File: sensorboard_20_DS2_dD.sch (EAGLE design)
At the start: 107 parts, among them IC1 ECMF02-2AMX6, IC2_ESP32S2WROOMM22S2 ESP32-S2-WROOM_M22S2H3200PH3Q0, IC4 TPA6211A1DRBR, J4_USB USB_CONN, J5_AUDIO SJ-3523-SMT-TR, J6_OAT 2.5mm JACK, J7 30310-6002HB, U1 LPS22HB, U10-MAG_SENSOR MMC5983MA, U11 LDL212PV33R, U12 NCV8163ASN330T1G, U13-I2C DS2482S-100+, U2 LPS22HB, U3-IMU LSM6DSMTR, U4 NCV8163ASN330T1G, U5 NCV8163ASN330T1G, U6 NCV8163ASN330T1G, U7 NCV8163ASN330T1G

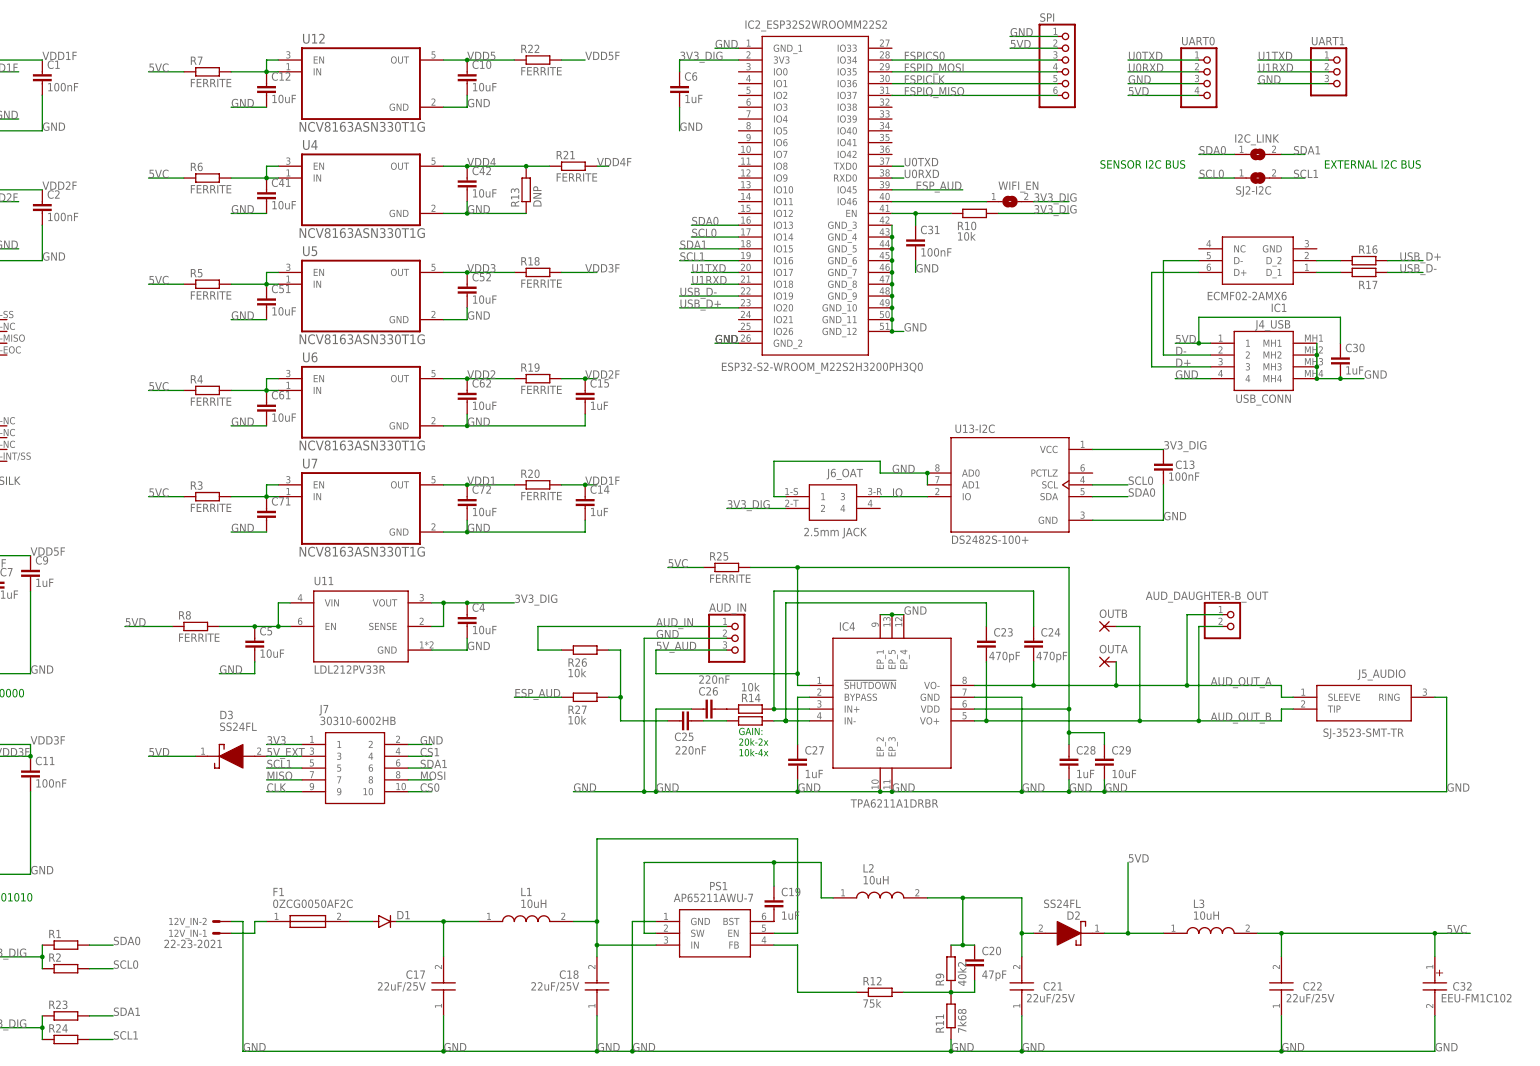
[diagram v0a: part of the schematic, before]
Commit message: Upload v20 files
Extend UART0 connector with EN, GPIO0 pins (Fixes #2)
Move ESP_AUD, WIFI_EN to different ESP32 pins (Fixes #3)
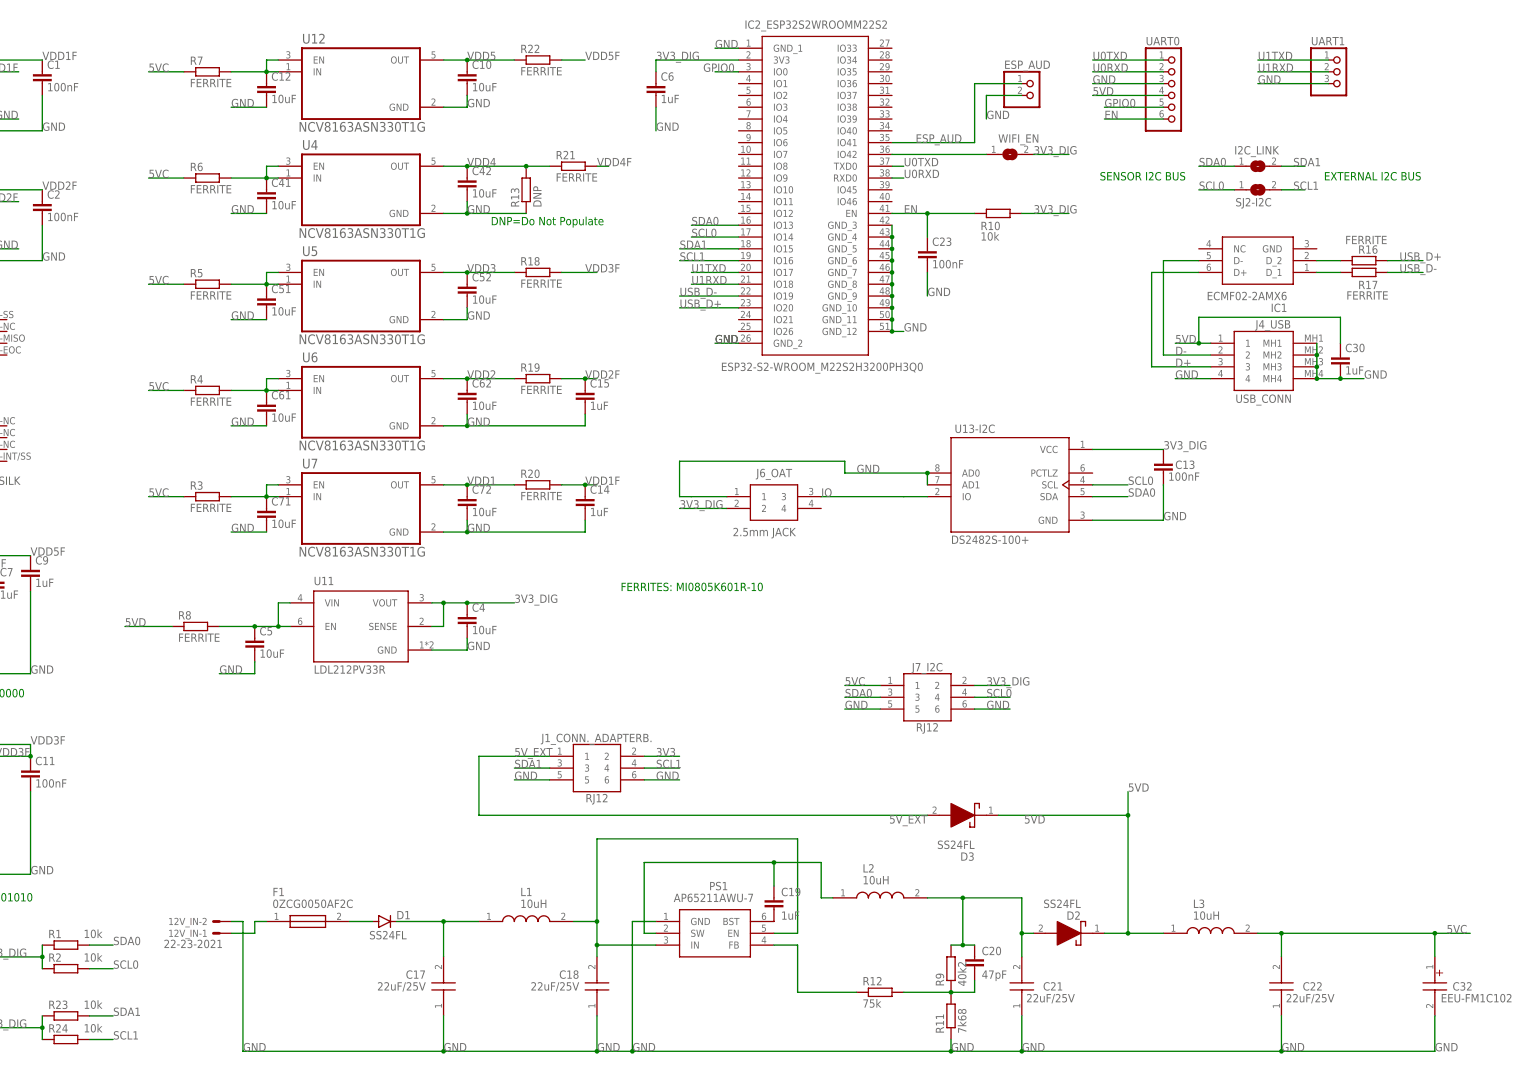
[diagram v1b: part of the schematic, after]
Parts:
- removed AUD_DAUGHTER-B_OUT: (no value), pinhead:PINHD-1X2
- removed AUD_IN: (no value), pinhead:PINHD-1X3
- removed C24: 470pF, rcl:C-EUC0805
- removed C25, C26: 220nF, rcl:C-EUC1206
- removed C27, C28: 1uF, rcl:C-EUC1206
- removed C29: 10uF, rcl:C-EUC1206
- removed C31: 100nF, rcl:C-EUC0603
- removed IC4: TPA6211A1DRBR, SamacSys_Parts:TPA6211A1DRBR
- removed J5_AUDIO: SJ-3523-SMT-TR, SamacSys_Parts:SJ-3523-SMT-TR
- removed J7: 30310-6002HB, SamacSys_Parts:30310-6002HB
- removed OUTA, OUTB: (no value), wirepad_SMALL:SMD2_SMALLSMALL
- removed R14, R26, R27: 10k, rcl:R-EU_R0805
- removed R15: (no value), rcl:R-EU_R0805
- removed R25: FERRITE, rcl:R-EU_R0805
- removed SPI: (no value), pinhead_dD:PINHD-1X6
- added ESP_AUD: (no value), pinhead:PINHD-1X2
- added J1_CONN._ADAPTERB., J7_I2C: RJ12, Sensor_Board_DS2:SAMACSYS_615006138421"
- C23: value 470pF -> 100nF
- C71: value (none) -> 10uF
- D1: value (none) -> SS24FL
- R1, R2, R23, R24: value (none) -> 10k
- R16, R17: value (none) -> FERRITE
- U$4: value (none) -> 4515DO-DS3BK030DPL
- UART0: device pinhead:PINHD-1X4 -> pinhead_dD:PINHD-1X6
- renumbered DLHR-L30G-E1BD-C-NAV8 to U$3
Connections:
- removed net 5V_AUD: AUD_IN.3, C28.1, C29.1, IC4.!SHUTDOWN, IC4.VDD, R25.2
- removed net AUD_IN: AUD_IN.1, R26.1
- removed net AUD_OUT_A: AUD_DAUGHTER-B_OUT.1, C24.2, IC4.VO-, J5_AUDIO.SLEEVE, OUTA.P
- removed net AUD_OUT_B: AUD_DAUGHTER-B_OUT.2, C23.2, IC4.VO+, J5_AUDIO.TIP, OUTB.P
- removed net CLK: J7.9
- removed net CS0: J7.10
- removed net CS1: J7.4
- removed net FSPICLK: IC2_ESP32S2WROOMM22S2.IO36, SPI.5
- removed net FSPICS0: IC2_ESP32S2WROOMM22S2.IO34, SPI.3
- removed net FSPID_MOSI: IC2_ESP32S2WROOMM22S2.IO35, SPI.4
- removed net FSPIQ_MISO: IC2_ESP32S2WROOMM22S2.IO37, SPI.6
- removed net MISO: J7.7
- removed net MOSI: J7.8
- removed net N$15: C25.1, R26.2, R27.2
- removed net N$21: C24.1, IC4.IN+, R14.2
- removed net N$22: C26.2, R14.1
- removed net N$23: C25.2, R15.1
- removed net N$25: IC2_ESP32S2WROOMM22S2.IO46, WIFI_EN.1
- removed net N$26: C27.1, IC4.BYPASS
- removed net N$7: C31.1, IC2_ESP32S2WROOMM22S2.EN, R10.1
- removed net N$8: C23.1, IC4.IN-, R15.2
- new net EN: C23.1, IC2_ESP32S2WROOMM22S2.EN, R10.1, UART0.6
- new net GPIO0: IC2_ESP32S2WROOMM22S2.IO0, UART0.5
- new net N$1: IC2_ESP32S2WROOMM22S2.IO42, WIFI_EN.1
- net 3V3: now also J1_CONN._ADAPTERB..2; no longer J7.1
- net 3V3_DIG: now also J7_I2C.2
- net 5VC: now also J7_I2C.1; no longer R25.1
- net 5VD: no longer SPI.2
- net 5V_EXT: now also J1_CONN._ADAPTERB..1; no longer J7.3
- net ESP_AUD: now also ESP_AUD.1, IC2_ESP32S2WROOMM22S2.IO41; no longer IC2_ESP32S2WROOMM22S2.IO45, R27.1
- net GND: now also C23.2, ESP_AUD.2, J1_CONN._ADAPTERB..5, J1_CONN._ADAPTERB..6, J7_I2C.5, J7_I2C.6; no longer AUD_IN.2, C26.1, C27.2, C28.2, C29.2, C31.2, IC4.EP_1, IC4.EP_2, IC4.EP_3, IC4.EP_4, IC4.EP_5, IC4.GND, J5_AUDIO.RING, J7.2, SPI.1
- net SCL0: now also J7_I2C.4
- net SCL1: now also J1_CONN._ADAPTERB..4; no longer J7.5
- net SDA0: now also J7_I2C.3
- net SDA1: now also J1_CONN._ADAPTERB..3; no longer J7.6
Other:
- note added: "DNP=Do Not Populate"
- note added: "FERRITES: MI0805K601R-10"
- note removed: "GAIN: 20k-2x 10k-4x"
- moved on the sheet: C23, C6, D3, I2C_LINK, J6_OAT, R10, SJ2-I2C, WIFI_EN
